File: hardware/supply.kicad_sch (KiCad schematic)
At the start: 34 parts, among them IC4 ACT4533AYH-T, U2 4011, U3 4081, U4 4071, U7 LM1117-3.3

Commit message: kurde no jeszcze nie skonczylem ale sune dalej
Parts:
- C21, C24, C25: footprint Capacitor_SMD:C_0603_1608Metric -> Capacitor_SMD:C_0603_1608Metric_Pad1.08x0.95mm_HandSolder
- C27, C28: footprint Capacitor_SMD:C_0201_0603Metric_Pad0.64x0.40mm_HandSolder -> Capacitor_SMD:C_0603_1608Metric_Pad1.08x0.95mm_HandSolder
- D10: footprint Diode_SMD:D_SMB -> Diode_SMD:D_SOD-323_HandSoldering
- R19, R26: footprint Resistor_SMD:R_1206_3216Metric -> Resistor_SMD:R_0603_1608Metric_Pad0.98x0.95mm_HandSolder
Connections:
- net critical_C is gone; now on net +24V: C17.1, C18.1, D7.1 (A1), F1.1, IC4.2 (IN)
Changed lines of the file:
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@@
   (junction (at 85.09 31.75) (diameter 0) (color 0 0 0 0)
   )
+  (junction (at 52.07 31.75) (diameter 0) (color 0 0 0 0)
+  )
   (junction (at 100.33 109.22) (diameter 0) (color 0 0 0 0)
   )
@@
     (stroke (width 0) (type default) (color 0 0 0 0))
   )
-  (wire (pts (xy 48.26 31.75) (xy 60.96 31.75))
+  (wire (pts (xy 48.26 31.75) (xy 52.07 31.75))
     (stroke (width 0) (type default) (color 0 0 0 0))
   )
@@
     (stroke (width 0) (type default) (color 0 0 0 0))
   )
+  (wire (pts (xy 52.07 31.75) (xy 52.07 29.21))
+    (stroke (width 0) (type default) (color 0 0 0 0))
+  )
   (wire (pts (xy 213.36 31.75) (xy 207.01 31.75))
     (stroke (width 0) (type default) (color 0 0 0 0))
@@
   )
   (wire (pts (xy 168.91 125.73) (xy 168.91 116.84))
+    (stroke (width 0) (type default) (color 0 0 0 0))
+  )
+  (wire (pts (xy 52.07 31.75) (xy 60.96 31.75))
     (stroke (width 0) (type default) (color 0 0 0 0))
   )
@@
     (effects (font (size 1.27 1.27) italic) (justify left bottom))
   )
-  (label "critical_C" (at 85.09 44.45 90)
-    (effects (font (size 0.7 0.7) italic) (justify left bottom))
-  )
   (label "SW_loop" (at 142.24 44.45 270)
     (effects (font (size 0.7 0.7) italic) (justify right bottom))
@@
       (effects (font (size 1.27 1.27)) (justify right))
     )
-    (property "Footprint" "Resistor_SMD:R_1206_3216Metric" (id 2) (at 114.808 134.62 90)
+    (property "Footprint" "Resistor_SMD:R_0603_1608Metric_Pad0.98x0.95mm_HandSolder" (id 2) (at 114.808 134.62 90)
       (effects (font (size 1.27 1.27)) hide)
     )
@@
       (effects (font (size 1.27 1.27)) (justify left))
     )
-    (property "Footprint" "Diode_SMD:D_SMB" (id 2) (at 199.39 134.62 0)
+    (property "Footprint" "Diode_SMD:D_SOD-323_HandSoldering" (id 2) (at 199.39 134.62 0)
       (effects (font (size 1.27 1.27)) hide)
     )
@@
       (effects (font (size 1.27 1.27)) (justify right))
     )
-    (property "Footprint" "Resistor_SMD:R_1206_3216Metric" (id 2) (at 208.788 57.15 90)
+    (property "Footprint" "Resistor_SMD:R_0603_1608Metric_Pad0.98x0.95mm_HandSolder" (id 2) (at 208.788 57.15 90)
       (effects (font (size 1.27 1.27)) hide)
     )
@@
       (effects (font (size 1.27 1.27)) (justify left))
     )
-    (property "Footprint" "Capacitor_SMD:C_0603_1608Metric" (id 2) (at 125.73 54.61 0)
+    (property "Footprint" "Capacitor_SMD:C_0603_1608Metric_Pad1.08x0.95mm_HandSolder" (id 2) (at 125.73 54.61 0)
       (effects (font (size 1.27 1.27)) hide)
     )
@@
       (effects (font (size 1.27 1.27)) (justify left))
     )
-    (property "Footprint" "Capacitor_SMD:C_0201_0603Metric_Pad0.64x0.40mm_HandSolder" (id 2) (at 214.3252 134.62 0)
+    (property "Footprint" "Capacitor_SMD:C_0603_1608Metric_Pad1.08x0.95mm_HandSolder" (id 2) (at 214.3252 134.62 0)
       (effects (font (size 1.27 1.27)) hide)
     )
@@
     (property "Reference" "C24" (id 0) (at 177.8 41.91 90))
     (property "Value" "1nF" (id 1) (at 177.8 44.45 90))
-    (property "Footprint" "Capacitor_SMD:C_0603_1608Metric" (id 2) (at 181.61 47.2948 0)
+    (property "Footprint" "Capacitor_SMD:C_0603_1608Metric_Pad1.08x0.95mm_HandSolder" (id 2) (at 181.61 47.2948 0)
       (effects (font (size 1.27 1.27)) hide)
     )
@@
     (property "Reference" "C25" (id 0) (at 180.34 59.69 90))
     (property "Value" "10uF" (id 1) (at 182.88 59.69 90))
-    (property "Footprint" "Capacitor_SMD:C_0603_1608Metric" (id 2) (at 185.7248 55.88 0)
+    (property "Footprint" "Capacitor_SMD:C_0603_1608Metric_Pad1.08x0.95mm_HandSolder" (id 2) (at 185.7248 55.88 0)
       (effects (font (size 1.27 1.27)) hide)
     )
@@
     (pin "1")
     (pin "2")
+  )
+  (symbol (lib_id "power:+24V") (at 52.07 29.21 0) (unit 1)
+    (in_bom yes) (on_board yes) (fields_autoplaced)
+    (property "Reference" "#PWR0110" (id 0) (at 52.07 33.02 0)
+      (effects (font (size 1.27 1.27)) hide)
+    )
+    (property "Value" "+24V" (id 1) (at 52.07 24.13 0))
+    (property "Footprint" "" (id 2) (at 52.07 29.21 0)
+      (effects (font (size 1.27 1.27)) hide)
+    )
+    (property "Datasheet" "" (id 3) (at 52.07 29.21 0)
+      (effects (font (size 1.27 1.27)) hide)
+    )
+    (pin "1")
   )
   (symbol (lib_id "Device:C") (at 60.96 127 0) (unit 1)
@@
       (effects (font (size 1.27 1.27)) (justify left))
     )
-    (property "Footprint" "Capacitor_SMD:C_0201_0603Metric_Pad0.64x0.40mm_HandSolder" (id 2) (at 244.8052 134.62 0)
-      (effects (font (size 1.27 1.27)) hide)
-    )
+    (property "Footprint" "Capacitor_SMD:C_0603_1608Metric_Pad1.08x0.95mm_HandSolder" (id 2) (at 244.8052 134.62 0)
+      (effects (font (size 1.27 1.27)) hide)
+    )

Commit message: fixed references addet tp;s mam pojutrze przejebany egzamin nara
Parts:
- C18: footprint Capacitor_SMD:C_0805_2012Metric_Pad1.18x1.45mm_HandSolder -> Capacitor_SMD:C_1206_3216Metric
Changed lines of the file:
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@@
       (effects (font (size 1.27 1.27)) (justify left))
     )
-    (property "Footprint" "Capacitor_SMD:C_0805_2012Metric_Pad1.18x1.45mm_HandSolder" (id 2) (at 86.0552 54.61 0)
+    (property "Footprint" "Capacitor_SMD:C_1206_3216Metric" (id 2) (at 86.0552 54.61 0)
       (effects (font (size 1.27 1.27)) hide)
     )

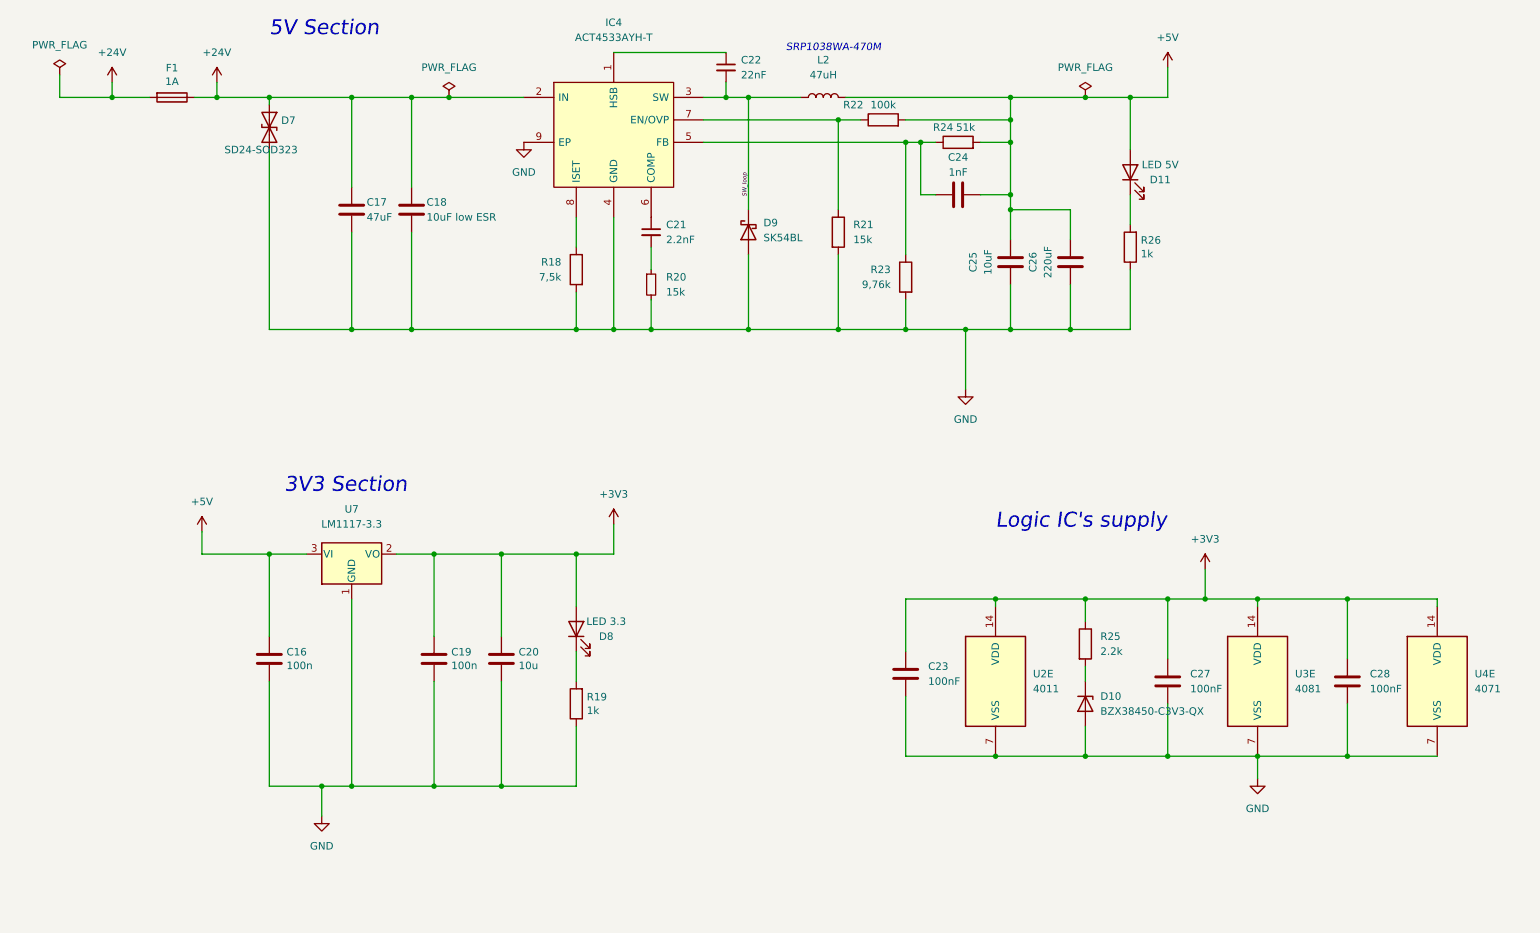
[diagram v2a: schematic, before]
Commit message: supply section redesign due to IC shortage
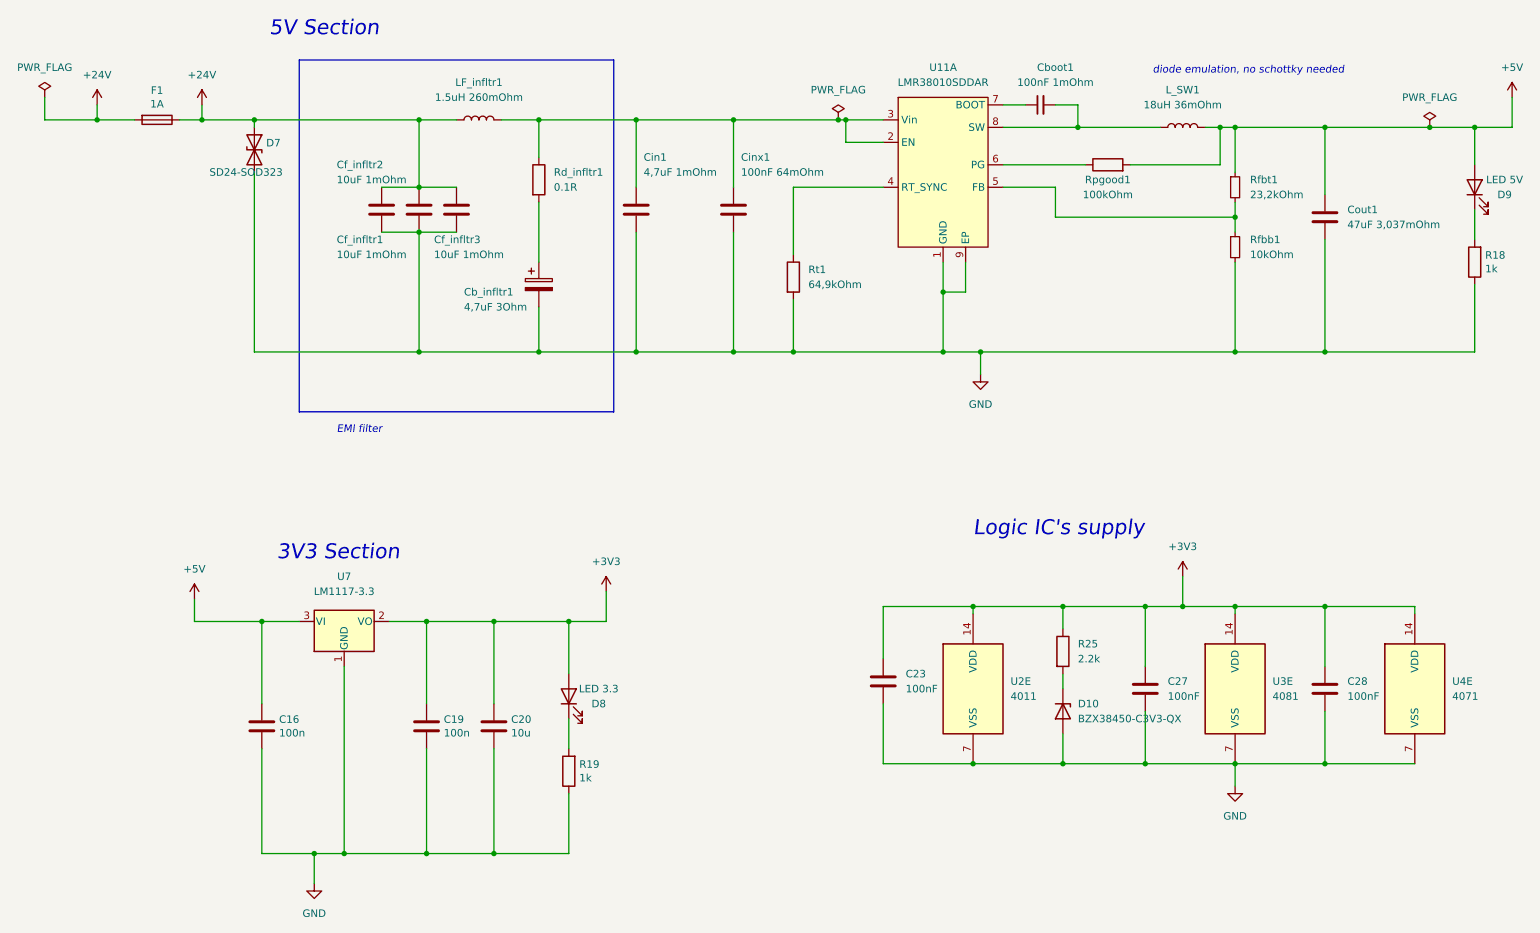
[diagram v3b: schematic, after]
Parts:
- removed C17: 47uF, Capacitor_SMD:CP_Elec_6.3x7.7, symbol Device:C
- removed C18: 10uF low ESR, Capacitor_SMD:C_1206_3216Metric, symbol Device:C
- removed C21: 2.2nF, Capacitor_SMD:C_0603_1608Metric_Pad1.08x0.95mm_HandSolder, symbol Device:C_Small
- removed C22: 22nF, Capacitor_SMD:C_1206_3216Metric, symbol Device:C_Small
- removed C24: 1nF, Capacitor_SMD:C_0603_1608Metric_Pad1.08x0.95mm_HandSolder, symbol Device:C
- removed C25: 10uF, Capacitor_SMD:C_0603_1608Metric_Pad1.08x0.95mm_HandSolder, symbol Device:C
- removed C26: 220uF, Capacitor_SMD:CP_Elec_6.3x7.7, symbol Device:C
- removed D11: LED 5V, LED_SMD:LED_0603_1608Metric_Pad1.05x0.95mm_HandSolder, symbol Device:LED
- removed D9: SK54BL, Diode_SMD:D_SMB, symbol Device:D_Schottky
- removed IC4: ACT4533AYH-T, SamacSys_Parts:SOIC127P600X170-9N, symbol SamacSys_Parts:ACT4533AYH-T
- removed L2: 47uH, PUTM_Kicad_FOOTPRINTS:L_Bourns_SRP1038WA, symbol Device:L
- removed R20: 15k, Resistor_SMD:R_0603_1608Metric_Pad0.98x0.95mm_HandSolder, symbol Device:R_Small
- removed R21: 15k, Resistor_SMD:R_0603_1608Metric_Pad0.98x0.95mm_HandSolder, symbol Device:R
- removed R22: 100k, Resistor_SMD:R_0603_1608Metric_Pad0.98x0.95mm_HandSolder, symbol Device:R
- removed R23: 9,76k, Resistor_SMD:R_0603_1608Metric_Pad0.98x0.95mm_HandSolder, symbol Device:R
- removed R24: 51k, Resistor_SMD:R_0603_1608Metric_Pad0.98x0.95mm_HandSolder, symbol Device:R
- removed R26: 1k, Resistor_SMD:R_0603_1608Metric_Pad0.98x0.95mm_HandSolder, symbol Device:R
- added Cb_infltr1: 4,7uF 3Ohm, Capacitor_SMD:CP_Elec_4x5.4, symbol Device:C_Polarized
- added Cboot1: 100nF 1mOhm, Capacitor_SMD:C_0402_1005Metric_Pad0.74x0.62mm_HandSolder, symbol Device:C_Small
- added Cf_infltr1, Cf_infltr2, Cf_infltr3: 10uF 1mOhm, Capacitor_SMD:C_1210_3225Metric_Pad1.33x2.70mm_HandSolder, symbol Device:C
- added Cin1: 4,7uF 1mOhm, Capacitor_SMD:C_0805_2012Metric_Pad1.18x1.45mm_HandSolder, symbol Device:C
- added Cinx1: 100nF 64mOhm, Capacitor_SMD:C_0805_2012Metric_Pad1.18x1.45mm_HandSolder, symbol Device:C
- added Cout1: 47uF 3,037mOhm, Capacitor_SMD:C_1206_3216Metric_Pad1.33x1.80mm_HandSolder, symbol Device:C
- added D9: LED 5V, LED_SMD:LED_0603_1608Metric_Pad1.05x0.95mm_HandSolder, symbol Device:LED
- added LF_infltr1: 1.5uH 260mOhm, Inductor_SMD:L_0805_2012Metric_Pad1.05x1.20mm_HandSolder, symbol Device:L
- added L_SW1: 18uH 36mOhm, PUTM_Kicad_FOOTPRINTS:L_Bourns_EBS, symbol Device:L
- added Rd_infltr1: 0.1R, Resistor_SMD:R_0603_1608Metric_Pad0.98x0.95mm_HandSolder, symbol Device:R
- added Rfbb1: 10kOhm, Resistor_SMD:R_0402_1005Metric_Pad0.72x0.64mm_HandSolder, symbol Device:R_Small
- added Rfbt1: 23,2kOhm, Resistor_SMD:R_0402_1005Metric_Pad0.72x0.64mm_HandSolder, symbol Device:R_Small
- added Rpgood1: 100kOhm, Resistor_SMD:R_0603_1608Metric_Pad0.98x0.95mm_HandSolder, symbol Device:R
- added Rt1: 64,9kOhm, Resistor_SMD:R_0603_1608Metric_Pad0.98x0.95mm_HandSolder, symbol Device:R
- added U11: LMR38010SDDAR, Package_SO:TI_SO-PowerPAD-8_ThermalVias, symbol PUTM_SYMBOLS:LMR38010SDDAR
- R18: value 7,5k -> 1k
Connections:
- net +24V: now also Cf_infltr1.1, Cf_infltr2.1, Cf_infltr3.1, LF_infltr1.1
- net +5V: now also Cout1.1, D9.2 (A), L_SW1.2, Rfbt1.1, Rpgood1.2
- net GND: now also R18.1, Cb_infltr1.2, Cf_infltr1.2, Cf_infltr2.2, Cf_infltr3.2, Cin1.2, Cinx1.2, Cout1.2, Rfbb1.2, Rt1.2, U11.1 (GND), U11.9 (EP); no longer R18.2
- new net: D9.1 (K), R18.2
- new net: Cin1.1, Cinx1.1, LF_infltr1.2, Rd_infltr1.1, U11.2 (EN), U11.3 (Vin)
- new net: Rt1.1, U11.4 (RT_SYNC)
- new net: Rfbb1.1, Rfbt1.2, U11.5 (FB)
- new net: Rpgood1.1, U11.6 (PG)
- new net: Cboot1.1, U11.7 (BOOT)
- new net: Cboot1.2, L_SW1.1, U11.8 (SW)
- new net: Cb_infltr1.1, Rd_infltr1.2
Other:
- note added: "EMI filter"
- note added: "diode emulation, no schottky needed"
- note removed: "SRP1038WA-470M"
- moved on the sheet: C16, C19, C20, C23, C27, C28, D10, D8, R19, R25, U2E, U3E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
